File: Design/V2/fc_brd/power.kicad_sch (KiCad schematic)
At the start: 49 parts, among them J1 MCU Power, J2 Left Side Servo Power, J3 Right Side Servo Power, U1 STM32H747BIT6, U6 LD39200PU33R

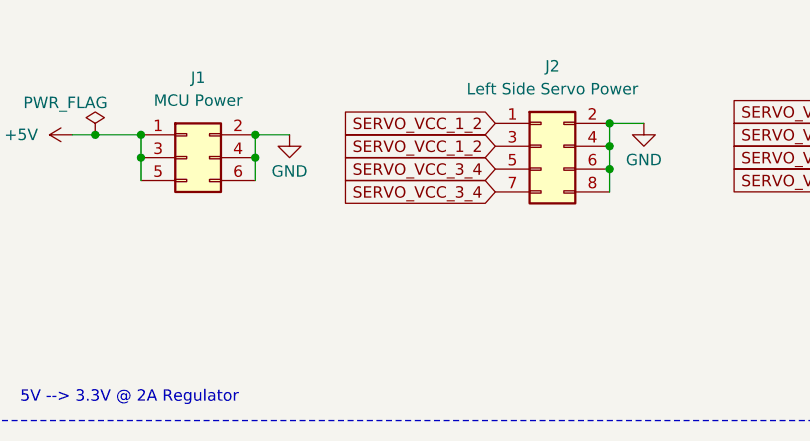
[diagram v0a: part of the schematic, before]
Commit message: layout changed to main fc board
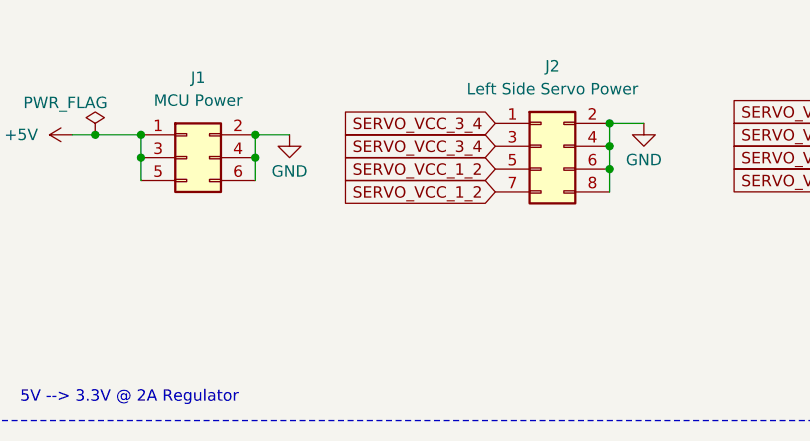
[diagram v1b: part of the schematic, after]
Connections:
- net SERVO_VCC_1_2: now also J2.5 (Pin_5), J2.7 (Pin_7); no longer J2.1 (Pin_1), J2.3 (Pin_3)
- net SERVO_VCC_3_4: now also J2.1 (Pin_1), J2.3 (Pin_3); no longer J2.5 (Pin_5), J2.7 (Pin_7)
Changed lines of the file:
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@@
 	(global_label "SERVO_VCC_1_2"
 		(shape input)
+		(at 83.82 43.18 180)
+		(fields_autoplaced yes)
+		(effects
+			(font
+				(size 1.27 1.27)
+			)
+			(justify right)
+		)
+		(property "Intersheetrefs" "${INTERSHEET_REFS}"
+			(at 65.8368 43.18 0)
+			(effects
+				(font
+					(size 1.27 1.27)
+				)
+				(justify right)
+				(hide yes)
+			)
+		)
+	)
+	(global_label "SERVO_VCC_1_2"
+		(shape input)
+		(at 83.82 40.64 180)
+		(fields_autoplaced yes)
+		(effects
+			(font
+				(size 1.27 1.27)
+			)
+			(justify right)
+		)
+		(property "Intersheetrefs" "${INTERSHEET_REFS}"
+			(at 65.8368 40.64 0)
+			(effects
+				(font
+					(size 1.27 1.27)
+				)
+				(justify right)
+				(hide yes)
+			)
+		)
+	)
+	(global_label "SERVO_VCC_5_6"
+		(shape input)
+		(at 127 36.83 180)
+		(fields_autoplaced yes)
+		(effects
+			(font
+				(size 1.27 1.27)
+			)
+			(justify right)
+		)
+		(property "Intersheetrefs" "${INTERSHEET_REFS}"
+			(at 109.0168 36.83 0)
+			(effects
+				(font
+					(size 1.27 1.27)
+				)
+				(justify right)
+				(hide yes)
+			)
+		)
+	)
+	(global_label "SERVO_VCC_3_4"
+		(shape input)
+		(at 83.82 35.56 180)
+		(fields_autoplaced yes)
+		(effects
+			(font
+				(size 1.27 1.27)
+			)
+			(justify right)
+		)
+		(property "Intersheetrefs" "${INTERSHEET_REFS}"
+			(at 65.8368 35.56 0)
+			(effects
+				(font
+					(size 1.27 1.27)
+				)
+				(justify right)
+				(hide yes)
+			)
+		)
+	)
+	(global_label "SERVO_VCC_5_6"
+		(shape input)
+		(at 127 34.29 180)
+		(fields_autoplaced yes)
+		(effects
+			(font
+				(size 1.27 1.27)
+			)
+			(justify right)
+		)
+		(property "Intersheetrefs" "${INTERSHEET_REFS}"
+			(at 109.0168 34.29 0)
+			(effects
+				(font
+					(size 1.27 1.27)
+				)
+				(justify right)
+				(hide yes)
+			)
+		)
+	)
+	(global_label "VDD12DSI"
+		(shape input)
+		(at 48.26 236.22 90)
+		(fields_autoplaced yes)
+		(effects
+			(font
+				(size 1.27 1.27)
+			)
+			(justify left)
+		)
+		(property "Intersheetrefs" "${INTERSHEET_REFS}"
+			(at 48.26 224.1029 90)
+			(effects
+				(font
+					(size 1.27 1.27)
+				)
+				(justify left)
+				(hide yes)
+			)
+		)
+	)
+	(global_label "SERVO_VCC_7_8"
+		(shape input)
+		(at 127 41.91 180)
+		(fields_autoplaced yes)
+		(effects
+			(font
+				(size 1.27 1.27)
+			)
+			(justify right)
+		)
+		(property "Intersheetrefs" "${INTERSHEET_REFS}"
+			(at 109.0168 41.91 0)
+			(effects
+				(font
+					(size 1.27 1.27)
+				)
+				(justify right)
+				(hide yes)
+			)
+		)
+	)
+	(global_label "VDDA_MCU"
+		(shape input)
+		(at 146.05 213.36 0)
+		(fields_autoplaced yes)
+		(effects
+			(font
+				(size 1.27 1.27)
+			)
+			(justify left)
+		)
+		(property "Intersheetrefs" "${INTERSHEET_REFS}"
+			(at 158.7719 213.36 0)
+			(effects
+				(font
+					(size 1.27 1.27)
+				)
+				(justify left)
+				(hide yes)
+			)
+		)
+	)
+	(global_label "SERVO_VCC_7_8"
+		(shape input)
+		(at 127 39.37 180)
+		(fields_autoplaced yes)
+		(effects
+			(font
+				(size 1.27 1.27)
+			)
+			(justify right)
+		)
+		(property "Intersheetrefs" "${INTERSHEET_REFS}"
+			(at 109.0168 39.37 0)
+			(effects
+				(font
+					(size 1.27 1.27)
+				)
+				(justify right)
+				(hide yes)
+			)
+		)
+	)
+	(global_label "VDD12DSI"
+		(shape input)
+		(at 154.94 237.49 0)
+		(fields_autoplaced yes)
+		(effects
+			(font
+				(size 1.27 1.27)
+			)
+			(justify left)
+		)
+		(property "Intersheetrefs" "${INTERSHEET_REFS}"
+			(at 167.0571 237.49 0)
+			(effects
+				(font
+					(size 1.27 1.27)
+				)
+				(justify left)
+				(hide yes)
+			)
+		)
+	)
+	(global_label "SERVO_VCC_3_4"
+		(shape input)
 		(at 83.82 38.1 180)
 		(fields_autoplaced yes)
@@
 			(effects
 				(font
-					(size 1.27 1.27)
-				)
-				(justify right)
-				(hide yes)
-			)
-		)
-	)
-	(global_label "SERVO_VCC_1_2"
-		(shape input)
-		(at 83.82 35.56 180)
-		(fields_autoplaced yes)
-		(effects
-			(font
-				(size 1.27 1.27)
-			)
-			(justify right)
-		)
-		(property "Intersheetrefs" "${INTERSHEET_REFS}"
-			(at 65.8368 35.56 0)
-			(effects
-				(font
-					(size 1.27 1.27)
-				)
-				(justify right)
-				(hide yes)
-			)
-		)
-	)
-	(global_label "SERVO_VCC_5_6"
-		(shape input)
-		(at 127 36.83 180)
-		(fields_autoplaced yes)
-		(effects
-			(font
-				(size 1.27 1.27)
-			)
-			(justify right)
-		)
-		(property "Intersheetrefs" "${INTERSHEET_REFS}"
-			(at 109.0168 36.83 0)
-			(effects
-				(font
-					(size 1.27 1.27)
-				)
-				(justify right)
-				(hide yes)
-			)
-		)
-	)
-	(global_label "SERVO_VCC_3_4"
-		(shape input)
-		(at 83.82 40.64 180)
-		(fields_autoplaced yes)
-		(effects
-			(font
-				(size 1.27 1.27)
-			)
-			(justify right)
-		)
-		(property "Intersheetrefs" "${INTERSHEET_REFS}"
-			(at 65.8368 40.64 0)
-			(effects
-				(font
-					(size 1.27 1.27)
-				)
-				(justify right)
-				(hide yes)
-			)
-		)
-	)
-	(global_label "SERVO_VCC_5_6"
-		(shape input)
-		(at 127 34.29 180)
-		(fields_autoplaced yes)
-		(effects
-			(font
-				(size 1.27 1.27)
-			)
-			(justify right)
-		)
-		(property "Intersheetrefs" "${INTERSHEET_REFS}"
-			(at 109.0168 34.29 0)
-			(effects
-				(font
-					(size 1.27 1.27)
-				)
-				(justify right)
-				(hide yes)
-			)
-		)
-	)
-	(global_label "VDD12DSI"
-		(shape input)
-		(at 48.26 236.22 90)
-		(fields_autoplaced yes)
-		(effects
-			(font
-				(size 1.27 1.27)
-			)
-			(justify left)
-		)
-		(property "Intersheetrefs" "${INTERSHEET_REFS}"
-			(at 48.26 224.1029 90)
-			(effects
-				(font
-					(size 1.27 1.27)
-				)
-				(justify left)
-				(hide yes)
-			)
-		)
-	)
-	(global_label "SERVO_VCC_7_8"
-		(shape input)
-		(at 127 41.91 180)
-		(fields_autoplaced yes)
-		(effects
-			(font
-				(size 1.27 1.27)
-			)
-			(justify right)
-		)
-		(property "Intersheetrefs" "${INTERSHEET_REFS}"
-			(at 109.0168 41.91 0)
-			(effects
-				(font
-					(size 1.27 1.27)
-				)
-				(justify right)
-				(hide yes)
-			)
-		)
-	)
-	(global_label "VDDA_MCU"
-		(shape input)
-		(at 146.05 213.36 0)
-		(fields_autoplaced yes)
-		(effects
-			(font
-				(size 1.27 1.27)
-			)
-			(justify left)
-		)
-		(property "Intersheetrefs" "${INTERSHEET_REFS}"
-			(at 158.7719 213.36 0)
-			(effects
-				(font
-					(size 1.27 1.27)
-				)
-				(justify left)
-				(hide yes)
-			)
-		)
-	)
-	(global_label "SERVO_VCC_7_8"
-		(shape input)
-		(at 127 39.37 180)
-		(fields_autoplaced yes)
-		(effects
-			(font
-				(size 1.27 1.27)
-			)
-			(justify right)
-		)
-		(property "Intersheetrefs" "${INTERSHEET_REFS}"
-			(at 109.0168 39.37 0)
-			(effects
-				(font
-					(size 1.27 1.27)
-				)
-				(justify right)
-				(hide yes)
-			)
-		)
-	)
-	(global_label "VDD12DSI"
-		(shape input)
-		(at 154.94 237.49 0)
-		(fields_autoplaced yes)
-		(effects
-			(font
-				(size 1.27 1.27)
-			)
-			(justify left)
-		)
-		(property "Intersheetrefs" "${INTERSHEET_REFS}"
-			(at 167.0571 237.49 0)
-			(effects
-				(font
-					(size 1.27 1.27)
-				)
-				(justify left)
-				(hide yes)
-			)
-		)
-	)
-	(global_label "SERVO_VCC_3_4"
-		(shape input)
-		(at 83.82 43.18 180)
-		(fields_autoplaced yes)
-		(effects
-			(font
-				(size 1.27 1.27)
-			)
-			(justify right)
-		)
-		(property "Intersheetrefs" "${INTERSHEET_REFS}"
-			(at 65.8368 43.18 0)
-			(effects
-				(font

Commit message: completed main fc board layout
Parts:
- C13, C38: LCSC Part # C2907032 -> C15849
- FB1: footprint Lib:MPZ1005S121HT000 -> Inductor_SMD:L_0603_1608Metric_Pad1.05x0.95mm_HandSolder; PACKAGE_TYPE SMD 0402 -> SMD 0603
- J1, J2, J3: now left out of the parts list
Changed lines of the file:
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@@
 			)
 		)
-		(property "LCSC Part #" "C2907032"
+		(property "LCSC Part #" "C15849"
 			(at 222.25 191.77 0)
 			(effects
@@
 		(unit 1)
 		(exclude_from_sim no)
-		(in_bom yes)
+		(in_bom no)
 		(on_board yes)
 		(dnp no)
@@
 			)
 		)
-		(property "LCSC Part #" "C2907032"
+		(property "LCSC Part #" "C15849"
 			(at 184.15 267.97 0)
 			(effects
@@
 		(unit 1)
 		(exclude_from_sim no)
-		(in_bom yes)
+		(in_bom no)
 		(on_board yes)
 		(dnp no)
@@
 		(unit 1)
 		(exclude_from_sim no)
-		(in_bom yes)
+		(in_bom no)
 		(on_board yes)
 		(dnp no)
@@
 			)
 		)
-		(property "Footprint" "Lib:MPZ1005S121HT000"
+		(property "Footprint" "Inductor_SMD:L_0603_1608Metric_Pad1.05x0.95mm_HandSolder"
 			(at 215.9 189.738 90)
 			(effects
@@
 			)
 		)
-		(property "Datasheet" "MPZ1005S121HT000"
+		(property "Datasheet" "BLM18PG121SN1D"
 			(at 215.9 187.96 0)
 			(effects
@@
 			)
 		)
-		(property "Description" "120 Ohms @ 100 MHz 1 Power Line Ferrite Bead 0402 2A 55mOhm"
+		(property "Description" "120Ω@100MHz 2A 50mΩ"
 			(at 215.9 187.96 0)
 			(effects
@@
 			)
 		)
-		(property "PACKAGE_TYPE" "SMD 0402"
+		(property "PACKAGE_TYPE" "SMD 0603"
 			(at 215.9 187.96 90)
 			(effects

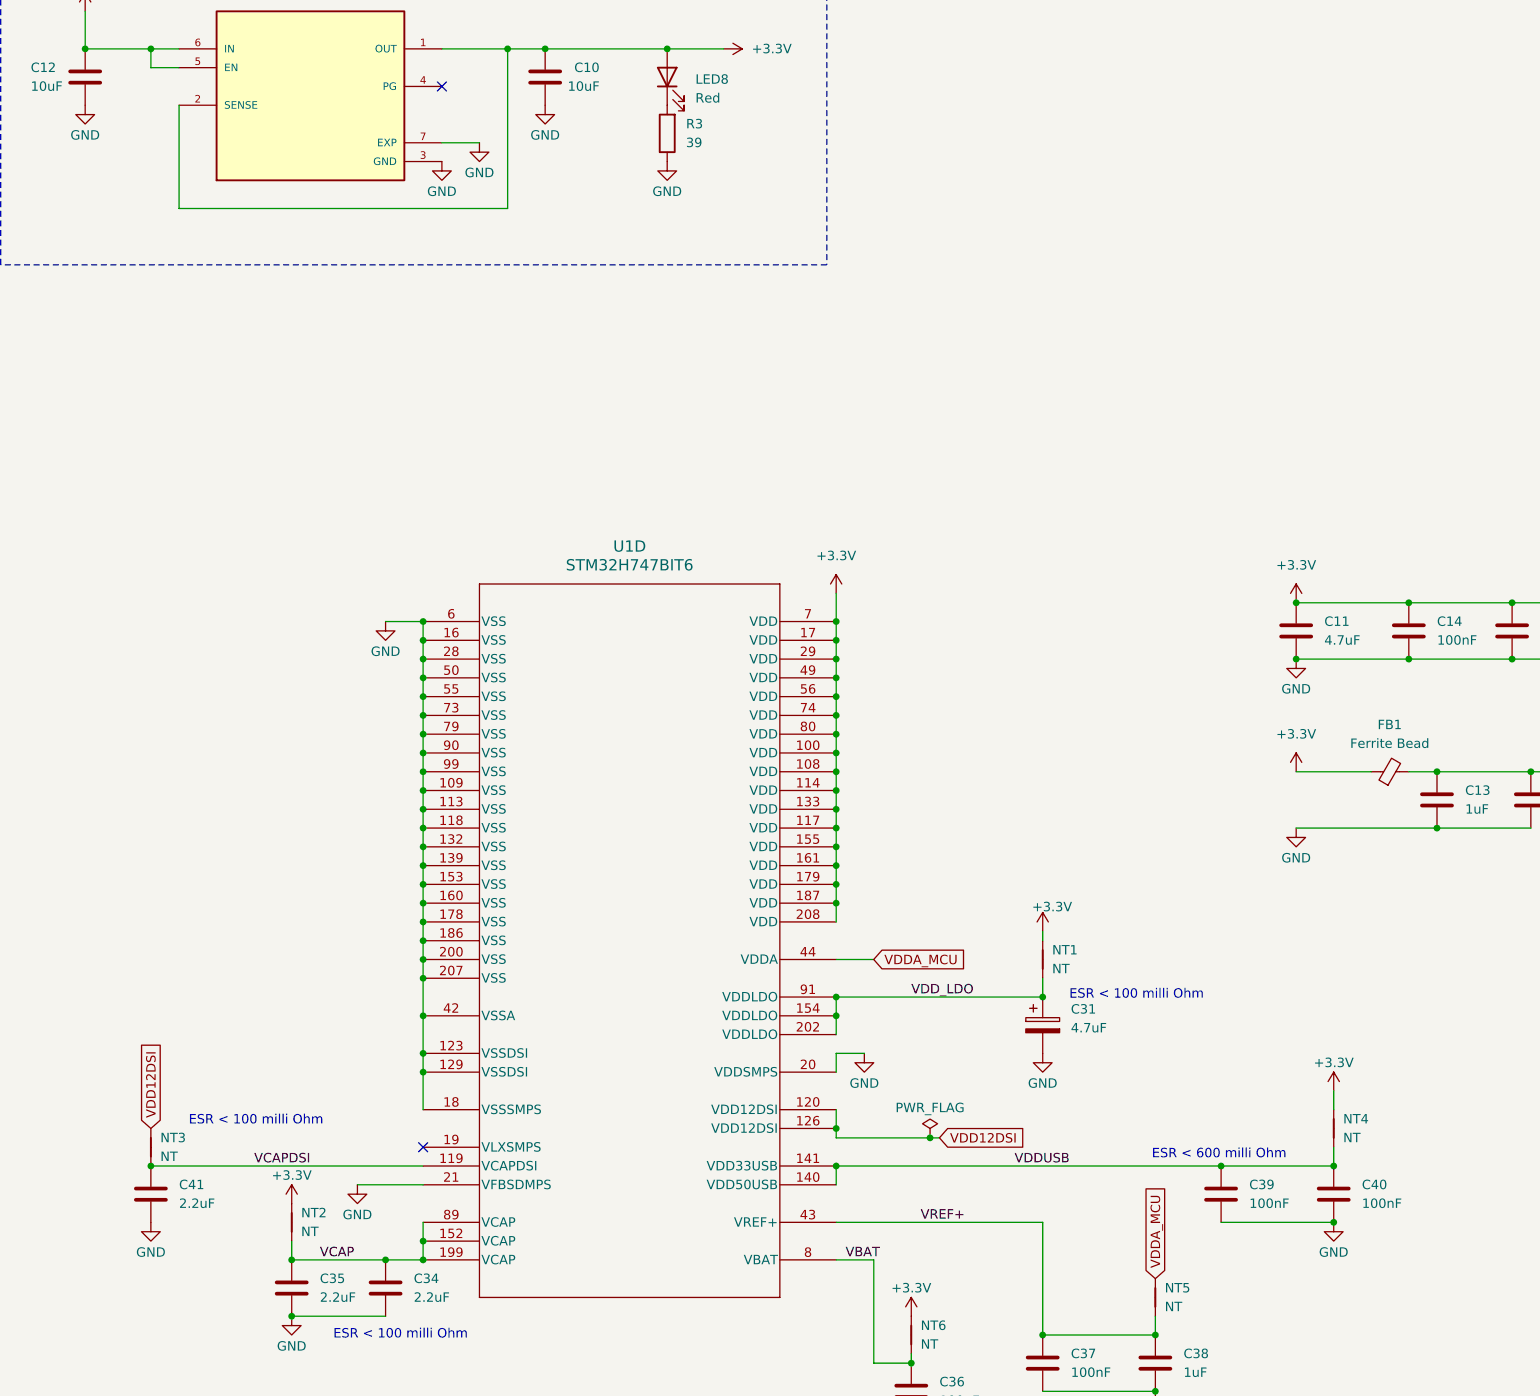
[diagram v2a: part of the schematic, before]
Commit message: VCORE is regulated with LDO instead of SMPS. Remove VCAP connection to 3.3V as VCAP is an output not an input
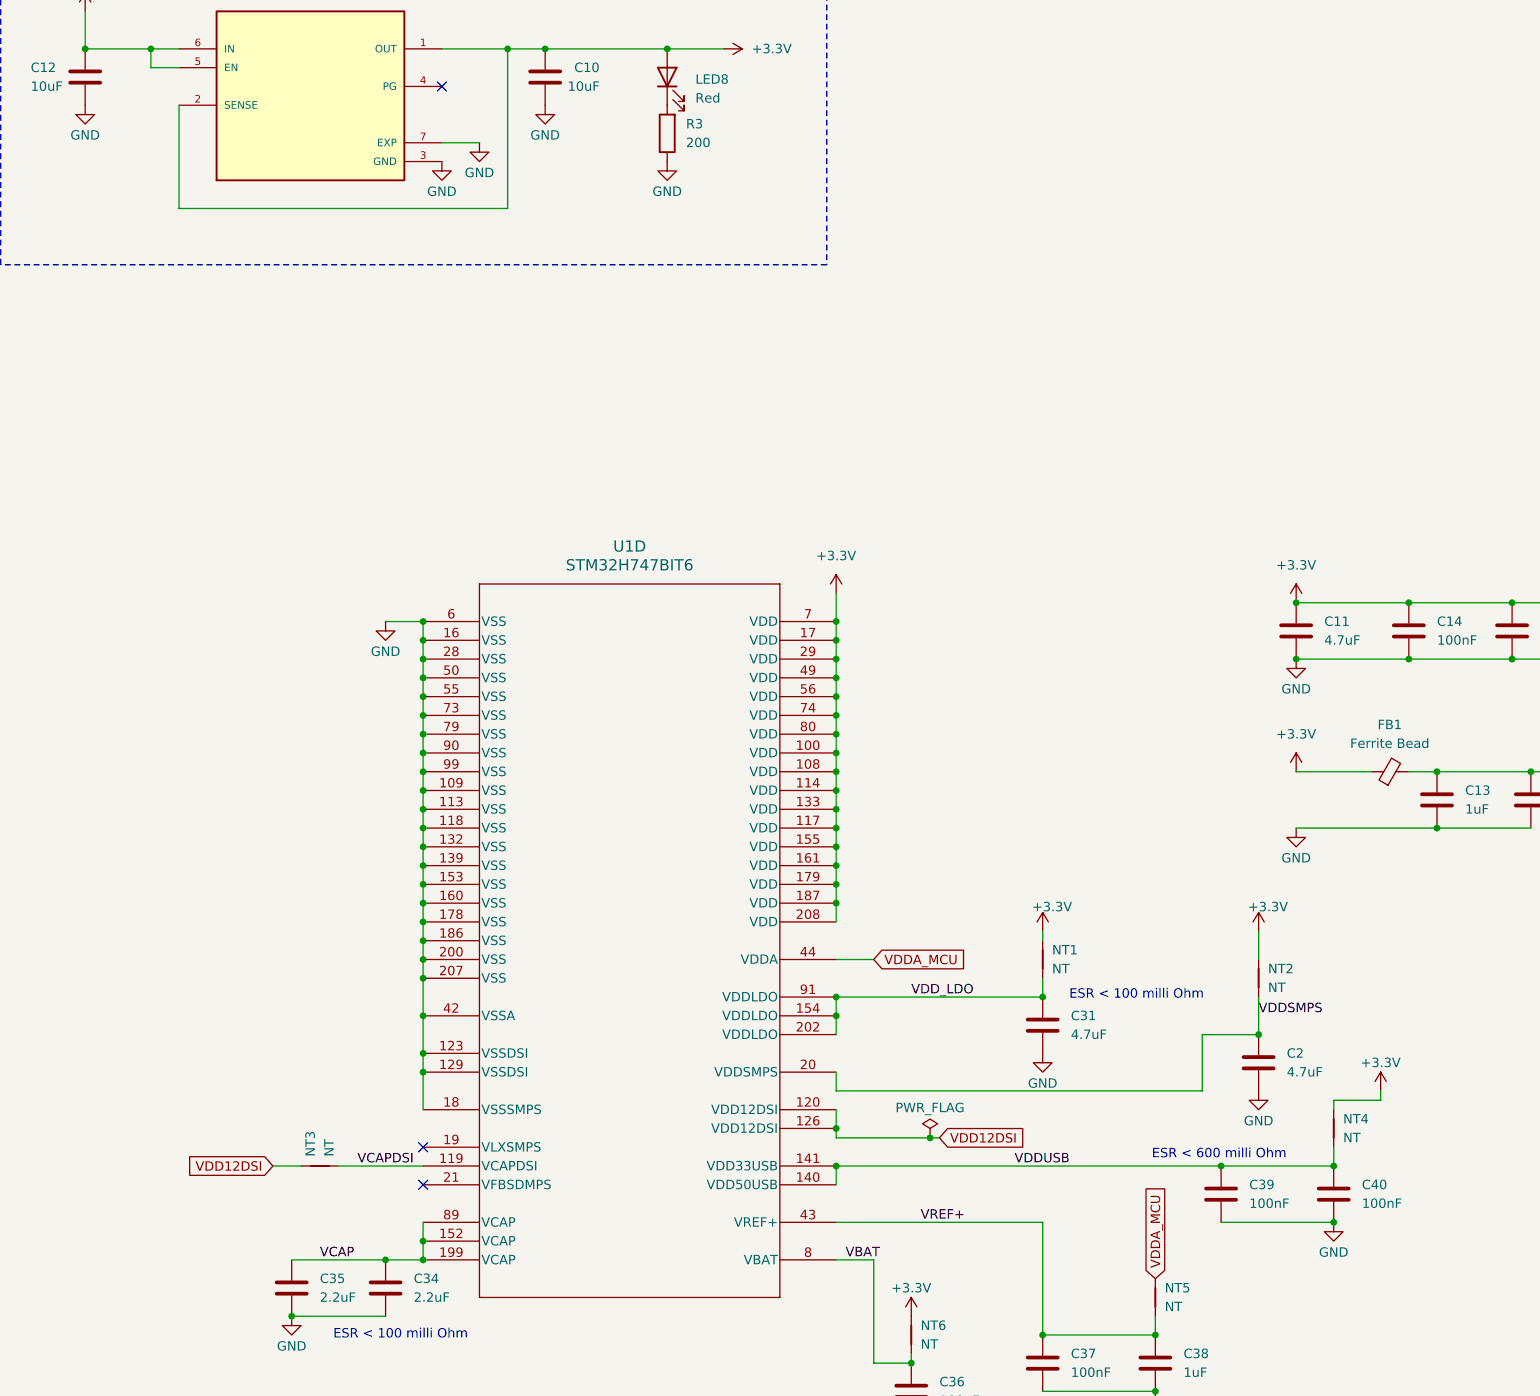
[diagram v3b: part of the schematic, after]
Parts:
- removed C41: 2.2uF, Capacitor_SMD:C_0603_1608Metric_Pad1.08x0.95mm_HandSolder, symbol Device:C
- added C2: 4.7uF, Capacitor_SMD:C_0603_1608Metric_Pad1.08x0.95mm_HandSolder, symbol Device:C
- C31: symbol Device:C_Polarized -> Device:C
- R3: value 39 -> 200; LCSC Part # C2907032 -> C8218; Manufacturer_Name FOJAN -> UNI-ROYAL(Uniroyal Elec); Manufacturer_Part_Number FRC0603F39R0TS -> 0603WAF2000T5E
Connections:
- net +3.3V: now also NT2.1; no longer NT2.2
- net GND: now also C2.2; no longer U1.20 (VDDSMPS), U1.21 (VFBSDMPS)
- net VCAP: no longer NT2.1
- net VCAPDSI: now also NT3.2; no longer NT3.1
- net VDD12DSI: now also NT3.1; no longer NT3.2
- new net VDDSMPS: C2.1, NT2.2, U1.20 (VDDSMPS)
- no-connect marks 2 -> 3
